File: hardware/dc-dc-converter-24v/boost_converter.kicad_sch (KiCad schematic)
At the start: 43 parts, among them Q1 SQJA42EP, Q2 SQJA42EP, Q3 SQJA42EP, Q4 SQJA42EP, U1 LM5176

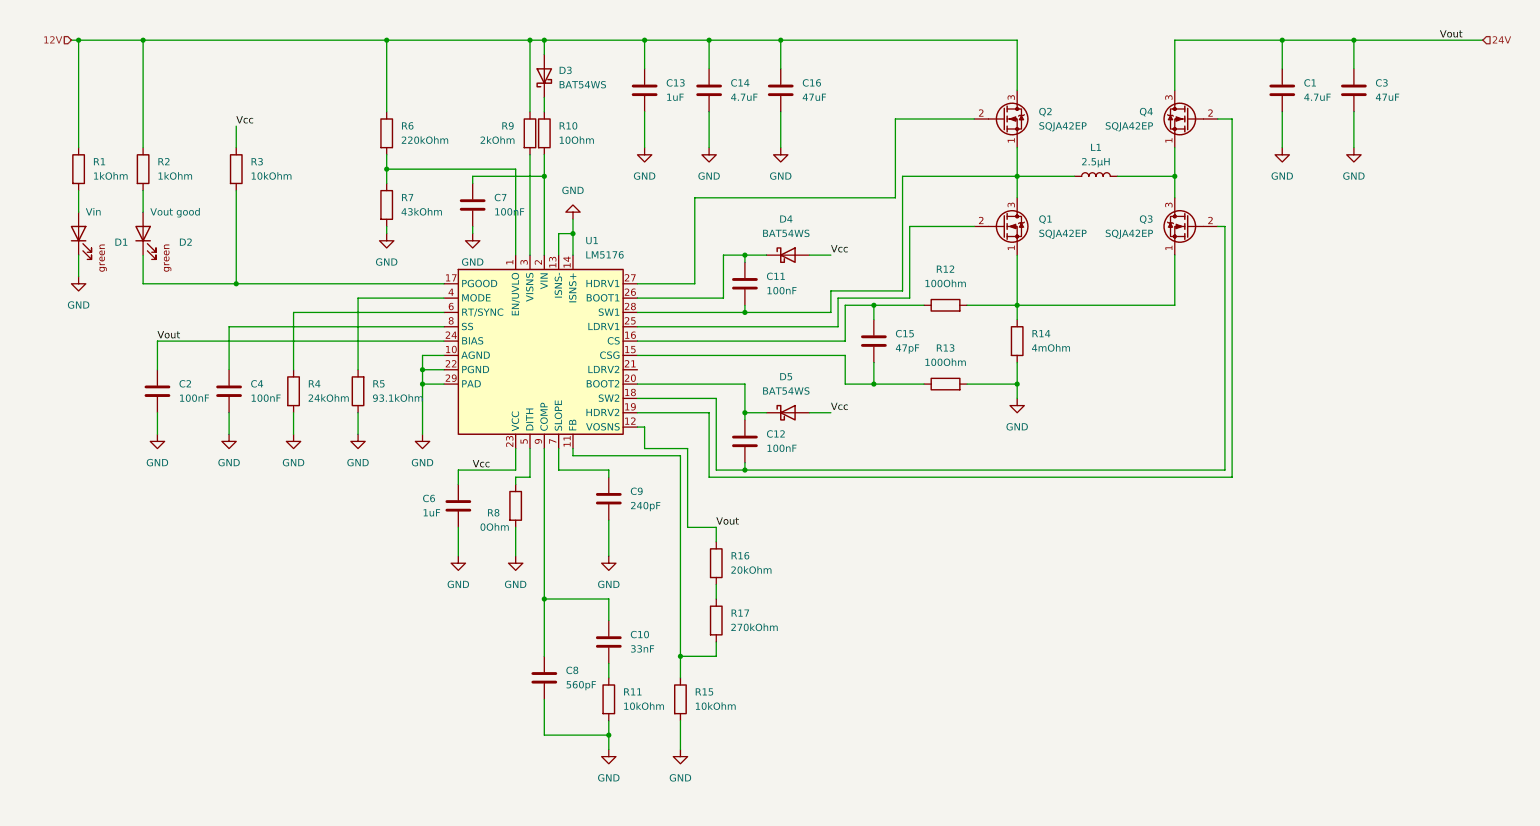
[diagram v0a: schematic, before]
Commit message: fix schematic error in DC-DC converter, add heatsink and mounting holes
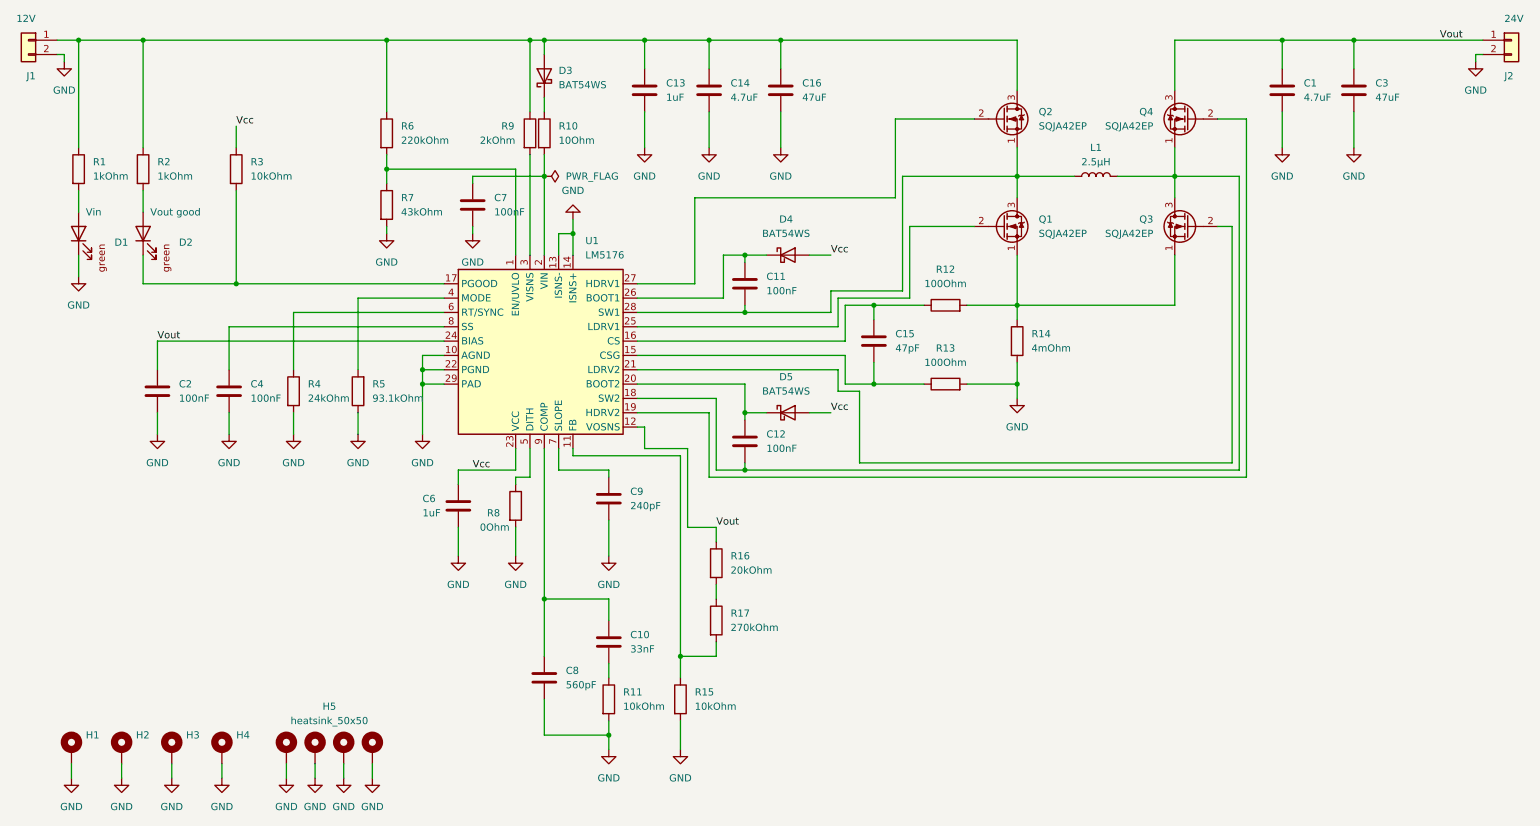
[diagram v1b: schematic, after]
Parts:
- added H1, H2, H3, H4: MountingHole_Pad_M6, benediktibk:MountingHole_6.4mm_M6_Pad_TopBottom, symbol benediktibk:MountingHole_Pad_M6
- added H5: heatsink_50x50, benediktibk:heatsink_50x50, symbol benediktibk:heatsink_50x50
- added J1: 12V, benediktibk:rspro_header_2pin_5_08mm, symbol benediktibk:rspro_header_2pin_5_08mm
- added J2: 24V, benediktibk:rspro_header_2pin_5_08mm, symbol benediktibk:rspro_header_2pin_5_08mm
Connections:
- net GND: now also H1.1, H2.1, H3.1, H4.1, H5.1 (GND), H5.2 (GND), H5.3 (GND), H5.4 (GND), J1.2 (Pin_2), J2.2 (Pin_2)
- net at L1.2, Q3.3 (D), Q4.1 (S): now also C12.2, U1.18 (SW2)
- net at U1.21 (LDRV2): now also Q3.2 (G)
- net 12V: no longer names the net of C13.1, C14.1, C16.1, D3.2 (A), Q2.3 (D), R1.1, R2.1, R6.1, R9.1
- net 12V: now also J1.1 (Pin_1)
- net 24V renamed Vout
- net Vout: now also J2.1 (Pin_1)

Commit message: create layout for DC-DC converter
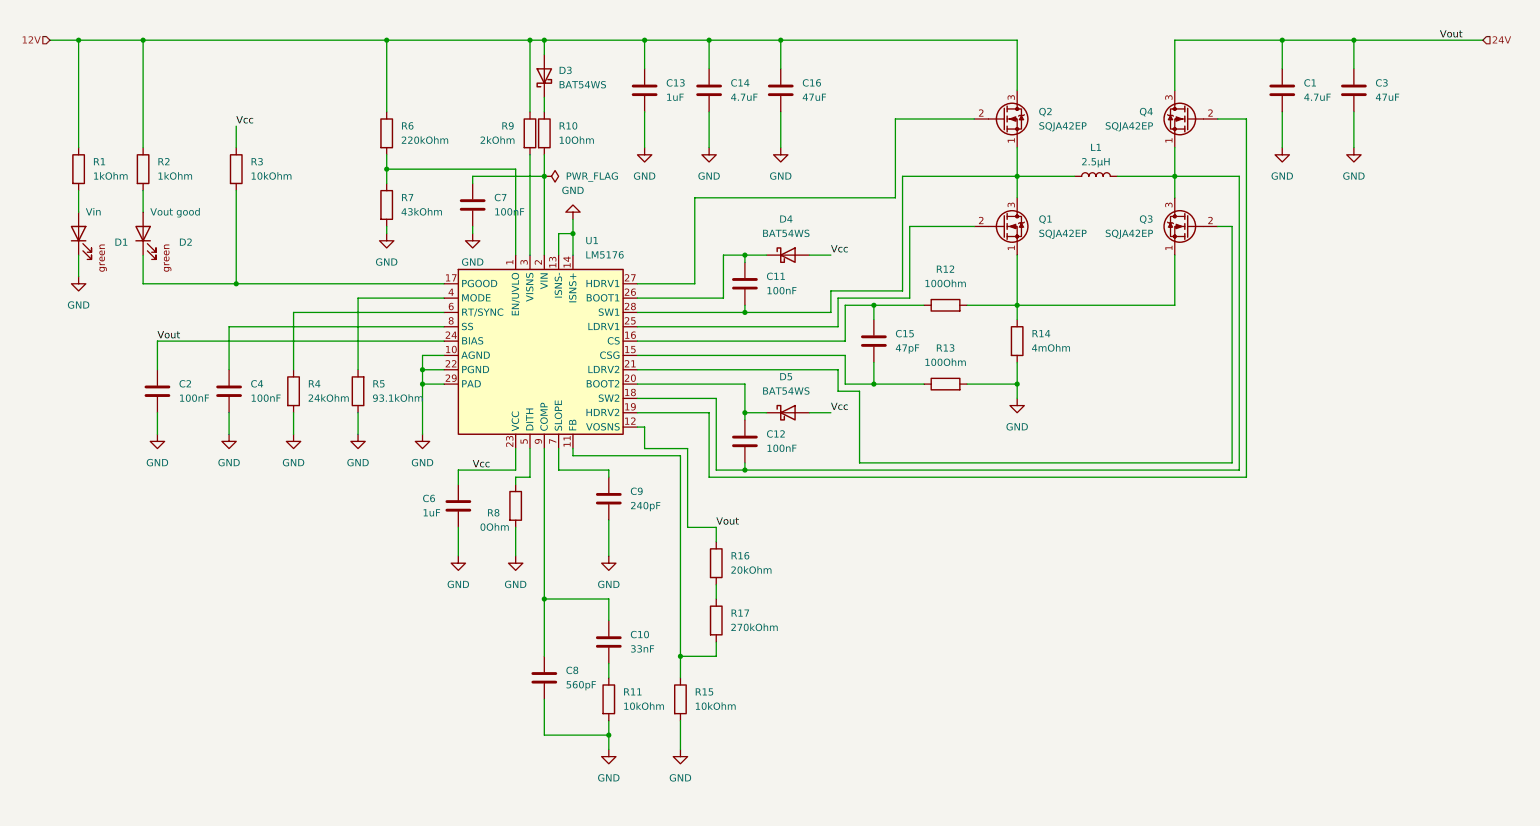
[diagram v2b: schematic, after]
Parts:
- removed H1, H2, H3, H4: MountingHole_Pad_M6, benediktibk:MountingHole_6.4mm_M6_Pad_TopBottom, symbol benediktibk:MountingHole_Pad_M6
- removed H5: heatsink_50x50, benediktibk:heatsink_50x50, symbol benediktibk:heatsink_50x50
- removed J1: 12V, benediktibk:rspro_header_2pin_5_08mm, symbol benediktibk:rspro_header_2pin_5_08mm
- removed J2: 24V, benediktibk:rspro_header_2pin_5_08mm, symbol benediktibk:rspro_header_2pin_5_08mm
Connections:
- net 12V: now reaches C13.1, C14.1, C16.1, D3.2 (A), Q2.3 (D), R1.1, R2.1, R6.1, R9.1
- net Vout renamed 24V

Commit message: fix RS order number
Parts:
- L1: RS order number 238-3683 -> 238-3683
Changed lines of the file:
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@@
       (effects (font (size 1.27 1.27)) hide)
     )
-    (property "RS order number" " 238-3683" (at 205.74 57.15 0)
+    (property "RS order number" "238-3683" (at 205.74 57.15 0)
       (effects (font (size 1.27 1.27)) hide)
     )
